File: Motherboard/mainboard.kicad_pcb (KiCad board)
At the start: 4 copper layers, 45 x 35 mm, 48 parts, among them IC1 BMX160, J1 Conn_01x01, J2 10118194-0001LF, J28 Conn_01x01, J29 Conn_01x01, J3 Micro_SD_Card, J30 Conn_01x01, J4 xf2m-2415-1a, J5 XF2M-1015-1A, SW1 KMR231NG LFS, U1 RFM95W-915S2, U2 ATSAMD51G_TQFN48, U3 DRV8848, U4 TPS82740BSIPR, U5 DRV8848, U6 MAX708RESA-T, U8 RFM95W-915S2, X1 ANTENNA_U.FL, X2 ANTENNA_U.FL

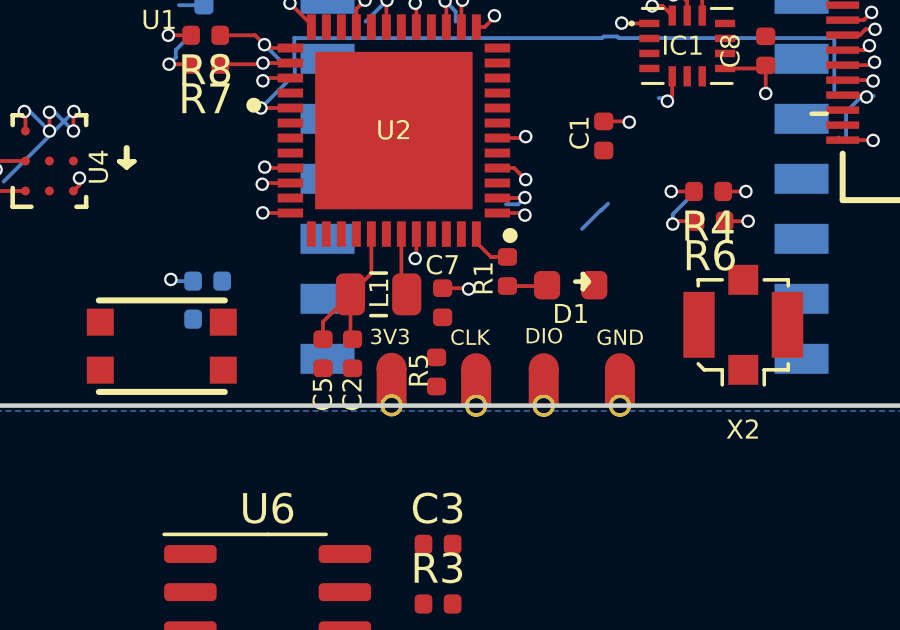
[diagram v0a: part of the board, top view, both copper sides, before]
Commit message: added traces for J29, J28, J30
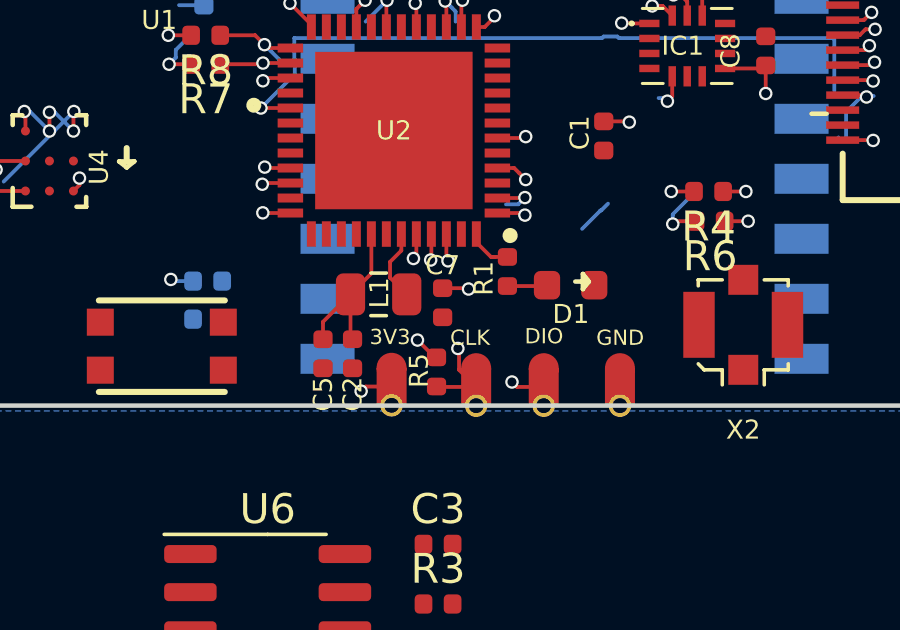
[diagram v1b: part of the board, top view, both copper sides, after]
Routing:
- net /SWCLK: track 0.00 -> 7.06 mm, vias 0 -> 2
- net /SWDIO: track 0.00 -> 6.97 mm, vias 0 -> 2
- net +3V3: track 18.4 -> 20.4 mm, vias 17 -> 19
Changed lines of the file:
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@@
     (thickness 1.2)
     (drawings 35)
-    (tracks 395)
+    (tracks 423)
     (zones 0)
     (modules 48)
@@
   (segment (start 82.9097 99.5086) (end 83.6295 99.5086) (width 0.127) (layer Top) (net 4))
   (segment (start 82.6597 99.2586) (end 82.9097 99.5086) (width 0.127) (layer Top) (net 4))
+  (segment (start 101.6889 108.4199) (end 101.5238 108.2548) (width 0.127) (layer Top) (net 5))
+  (via (at 101.5238 108.2548) (size 0.45) (drill 0.3) (layers Top Bottom) (net 5))
+  (segment (start 102.58298 108.4199) (end 101.6889 108.4199) (width 0.127) (layer Top) (net 5))
+  (segment (start 99.3368 104.1628) (end 99.3902 104.2162) (width 0.127) (layer Top) (net 5))
+  (segment (start 99.3368 103.3228) (end 99.3368 104.1628) (width 0.127) (layer Top) (net 5))
+  (via (at 99.3902 104.2162) (size 0.45) (drill 0.3) (layers Top Bottom) (net 5))
+  (segment (start 99.3902 106.1212) (end 101.5238 108.2548) (width 0.127) (layer In2.Cu) (net 5))
+  (segment (start 99.3902 104.2162) (end 99.3902 106.1212) (width 0.127) (layer In2.Cu) (net 5))
+  (segment (start 99.02458 108.4199) (end 99.0092 108.40452) (width 0.127) (layer Top) (net 6))
+  (segment (start 100.33 108.4199) (end 99.02458 108.4199) (width 0.127) (layer Top) (net 6))
+  (via (at 99.7204 107.1372) (size 0.45) (drill 0.3) (layers Top Bottom) (net 6))
+  (segment (start 99.75929 107.84919) (end 99.75929 107.17609) (width 0.127) (layer Top) (net 6))
+  (segment (start 99.75929 107.17609) (end 99.7204 107.1372) (width 0.127) (layer Top) (net 6))
+  (segment (start 100.33 108.4199) (end 99.75929 107.84919) (width 0.127) (layer Top) (net 6))
+  (via (at 98.813811 104.189379) (size 0.45) (drill 0.3) (layers Top Bottom) (net 6))
+  (segment (start 98.8368 104.16639) (end 98.813811 104.189379) (width 0.127) (layer Top) (net 6))
+  (segment (start 99.7204 107.1372) (end 98.813811 106.230611) (width 0.127) (layer In2.Cu) (net 6))
+  (segment (start 98.813811 106.230611) (end 98.813811 104.507577) (width 0.127) (layer In2.Cu) (net 6))
+  (segment (start 98.8368 103.3228) (end 98.8368 104.16639) (width 0.127) (layer Top) (net 6))
+  (segment (start 98.813811 104.507577) (end 98.813811 104.189379) (width 0.127) (layer In2.Cu) (net 6))
   (segment (start 100.8258 104.0868) (end 100.9514 104.0868) (width 0.127) (layer Top) (net 7))
   (segment (start 100.3368 103.5978) (end 100.8258 104.0868) (width 0.127) (layer Top) (net 7))
@@
   (segment (start 102.6643 105.0568) (end 102.6921 105.029) (width 0.127) (layer Top) (net 12))
   (segment (start 101.3714 105.0568) (end 102.6643 105.0568) (width 0.127) (layer Top) (net 12))
-  (segment (start 97.8368 105.1543) (end 98.0163 105.3338) (width 0.127) (layer Top) (net 18))
-  (segment (start 97.8368 103.3228) (end 97.8368 105.1543) (width 0.127) (layer Top) (net 18))
+  (segment (start 97.8368 103.8748) (end 97.460063 104.251537) (width 0.127) (layer Top) (net 18))
+  (segment (start 97.460063 104.251537) (end 97.460063 104.777563) (width 0.127) (layer Top) (net 18))
+  (segment (start 97.460063 104.777563) (end 98.0163 105.3338) (width 0.127) (layer Top) (net 18))
+  (segment (start 97.8368 103.3228) (end 97.8368 103.8748) (width 0.127) (layer Top) (net 18))
   (via (at 98.298 95.63101) (size 0.45) (drill 0.3) (layers Top Bottom) (net 20))
   (segment (start 98.3368 96.4228) (end 98.3368 95.66981) (width 0.127) (layer Top) (net 20))
   (segment (start 98.3368 95.66981) (end 98.298 95.63101) (width 0.127) (layer Top) (net 20))
-  (via (at 98.298 104.14) (size 0.45) (drill 0.3) (layers Top Bottom) (net 20))
-  (segment (start 98.3368 104.1012) (end 98.298 104.14) (width 0.127) (layer Top) (net 20))
-  (segment (start 98.3368 103.3228) (end 98.3368 104.1012) (width 0.127) (layer Top) (net 20))
   (via (at 101.981 100.076) (size 0.45) (drill 0.3) (layers Top Bottom) (net 20))
   (segment (start 101.9342 100.1228) (end 101.981 100.076) (width 0.127) (layer Top) (net 20))
@@
   (segment (start 107.6428 102.8954) (end 106.977622 102.8954) (width 0.127) (layer Top) (net 20))
   (segment (start 106.8832 102.6668) (end 106.8832 102.671624) (width 0.127) (layer Bottom) (net 20))
+  (via (at 98.3742 106.8578) (size 0.45) (drill 0.3) (layers Top Bottom) (net 20))
+  (segment (start 98.95092 107.43452) (end 98.3742 106.8578) (width 0.127) (layer Top) (net 20))
+  (segment (start 99.0092 107.43452) (end 98.95092 107.43452) (width 0.127) (layer Top) (net 20))
+  (via (at 96.4946 108.5596) (size 0.45) (drill 0.3) (layers Top Bottom) (net 20))
+  (segment (start 96.647 108.4072) (end 96.4946 108.5596) (width 0.127) (layer Top) (net 20))
+  (segment (start 97.5106 108.4072) (end 96.647 108.4072) (width 0.127) (layer Top) (net 20))
+  (segment (start 98.3368 103.3228) (end 98.3368 104.040464) (width 0.127) (layer Top) (net 20))
+  (via (at 98.239074 104.13819) (size 0.45) (drill 0.3) (layers Top Bottom) (net 20))
+  (segment (start 98.3368 104.040464) (end 98.239074 104.13819) (width 0.127) (layer Top) (net 20))
   (segment (start 83.909698 101.888798) (end 83.6295 101.6086) (width 0.127) (layer Top) (net 21))
   (segment (start 85.305999 101.888798) (end 83.909698 101.888798) (width 0.127) (layer Top) (net 21))

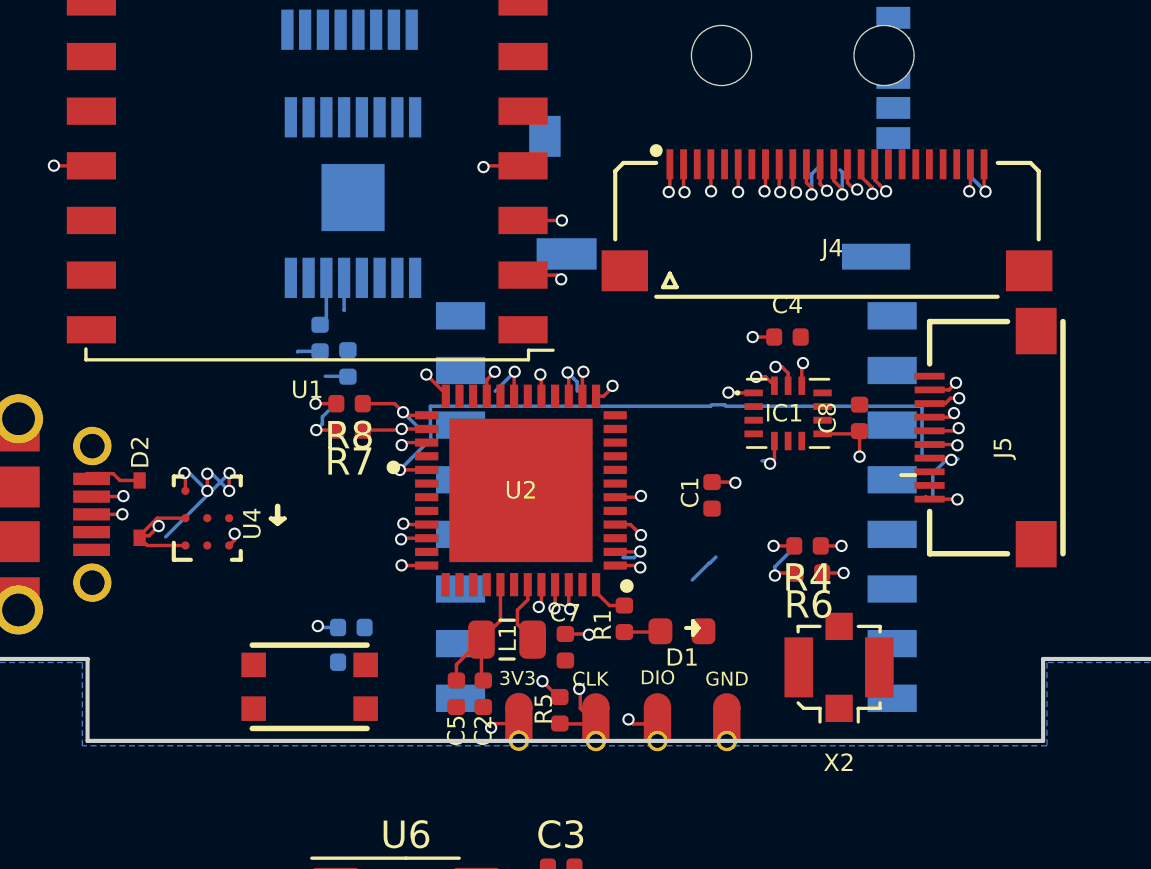
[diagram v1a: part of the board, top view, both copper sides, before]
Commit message: deleted accidental bottom traces on bottom of board
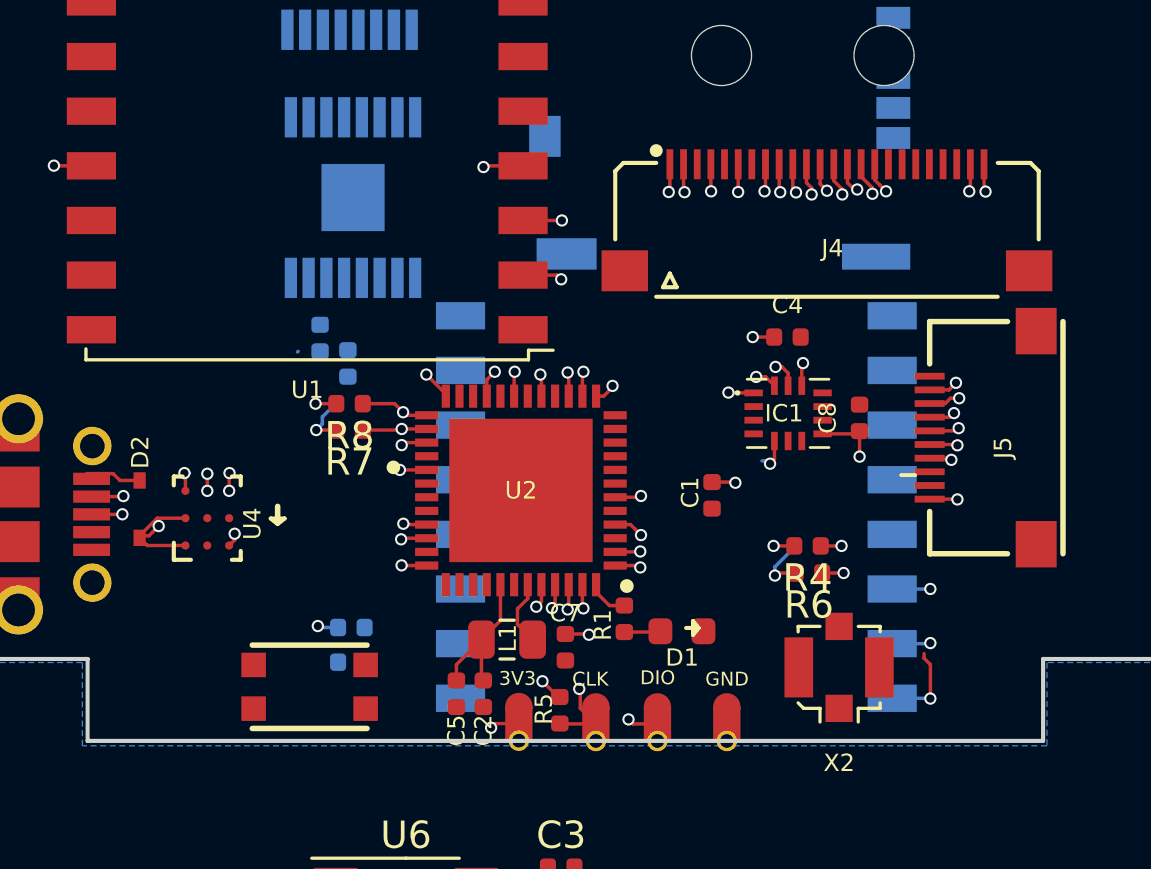
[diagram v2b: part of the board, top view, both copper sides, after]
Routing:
- net EN_CAM: track 45.4 -> 22.8 mm
- net Net-(D2-Pad1): track 20.4 -> 15.3 mm
- net RF_DIO2: track 0.00 -> 3.14 mm, vias 0 -> 1
- net GND: track 3.63 -> 0.82 mm
- net RF_DIO0: track 0.00 -> 2.28 mm, vias 0 -> 2
- net BATT_N: track 14.4 -> 12.3 mm
- net SCL2: track 5.49 -> 3.75 mm
- net Net-(C13-Pad2): track 1.82 -> 0.33 mm
- net RF_DIO1: track 0.00 -> 1.41 mm, vias 0 -> 1
- net SDA1: track 27.4 -> 26.2 mm
- net BURN2: track 2.37 -> 1.18 mm
- net MISO: track 17.4 -> 16.4 mm
- net RF_CS: track 1.91 -> 0.90 mm
- net BATT_P: track 14.5 -> 13.7 mm
- net SCL1: track 25.4 -> 24.6 mm

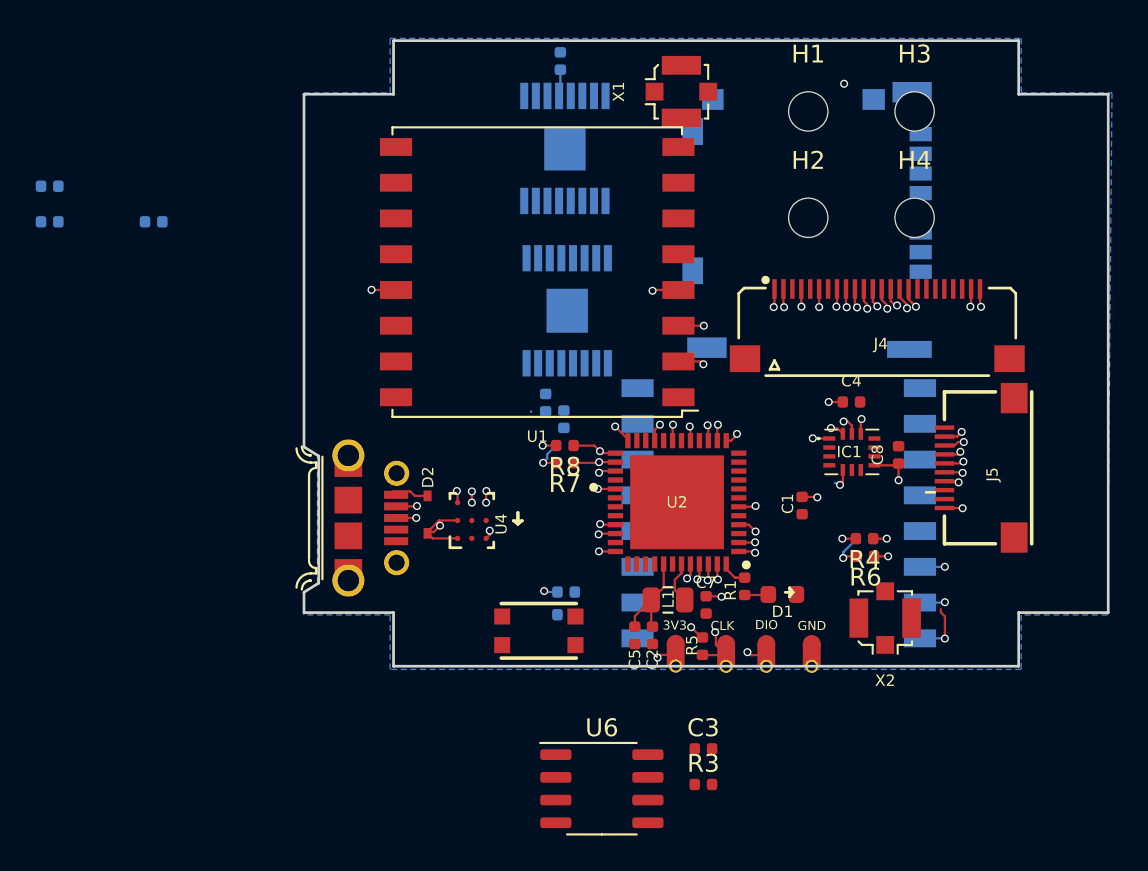
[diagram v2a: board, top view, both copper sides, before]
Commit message: updated position of UHF on bottom of board to not overlap MCU
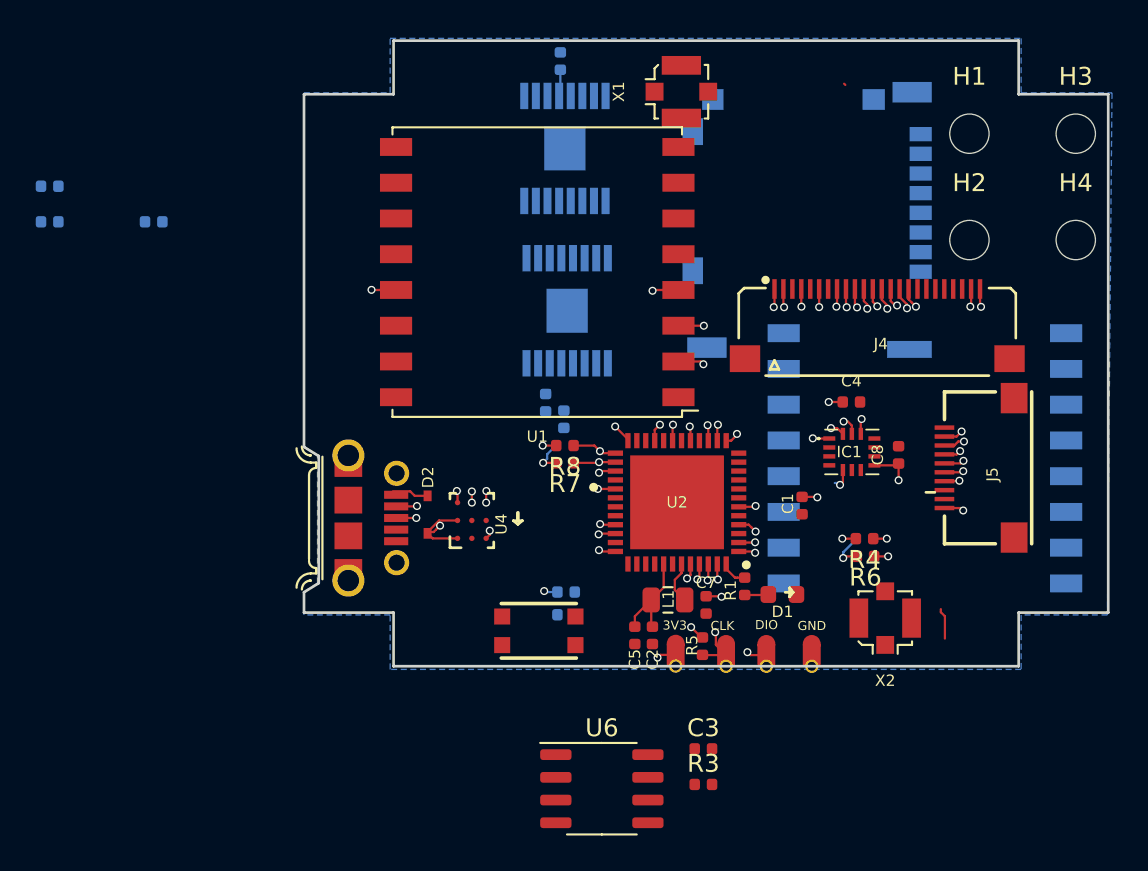
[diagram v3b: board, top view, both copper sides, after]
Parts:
- moved H3 9.10 mm to (119.9, 79.2)
- moved H4 9.10 mm to (119.9, 85.2)
- moved H1 9.10 mm to (113.9, 79.2)
- moved H2 9.10 mm to (113.9, 85.2)
- moved U8 8.74 mm to (111.5, 97.4)
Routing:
- net RF_DIO1: track 1.41 -> 0.00 mm, vias 1 -> 0
- net RF_DIO2: track 3.14 -> 1.74 mm, vias 1 -> 0
- net RF_DIO0: track 2.28 -> 0.88 mm, vias 2 -> 1
- net SDA1: track 26.2 -> 25.2 mm
- net SCL1: track 24.6 -> 23.9 mm
- net +3V3: vias 19 -> 18

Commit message: added watchdog timer footprint to PCB layout
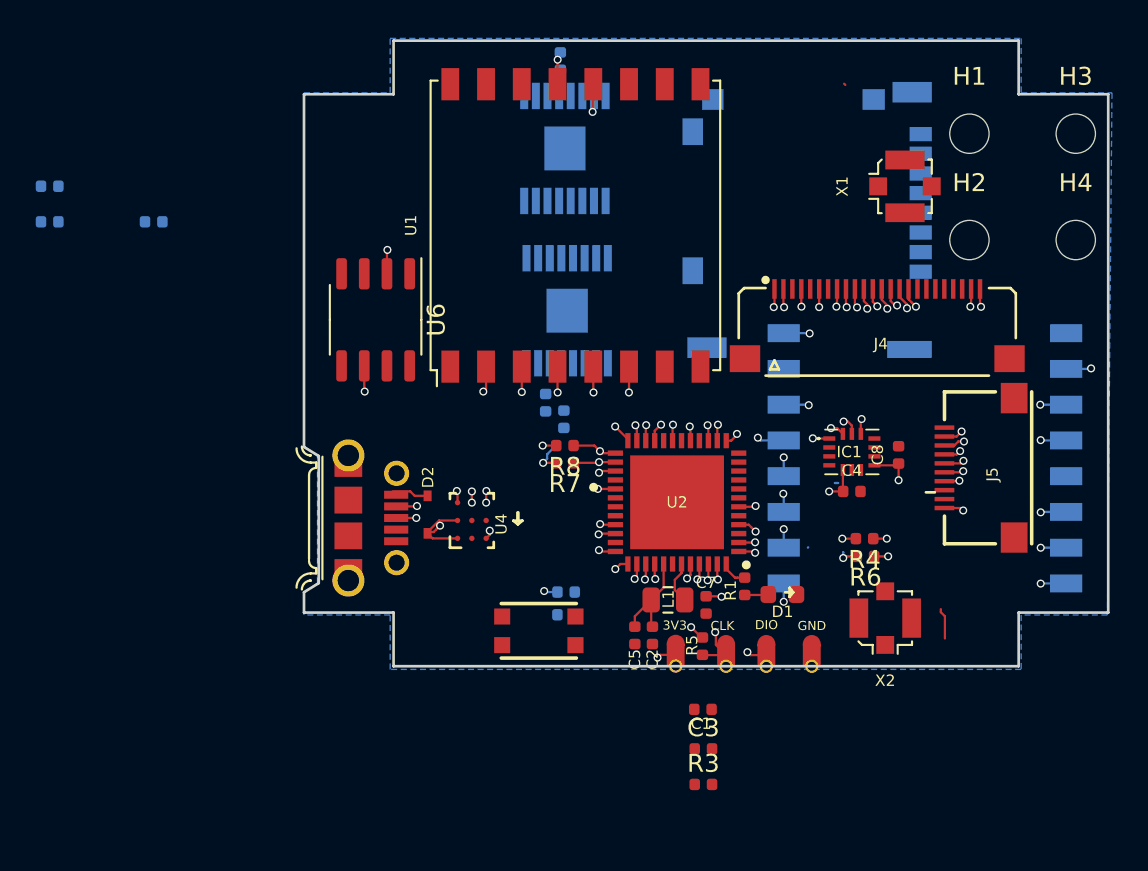
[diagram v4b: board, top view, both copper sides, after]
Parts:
- moved U6 29.1 mm to (80.7, 89.7), turned to 270 degrees
- moved X1 13.6 mm to (110.3, 82.2)
- moved C1 12.7 mm to (99.0, 111.5), turned to 0 degrees
- moved C4 5.00 mm to (107.4, 99.3)
- moved U1 3.37 mm to (91.9, 84.4), turned to 90 degrees
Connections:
- U2 pad 20: WDT_WDI -> Net-(U2-Pad20)
- U2 pad 37: Net-(U2-Pad37) -> WDT_WDI
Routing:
- net SCK: track 32.2 -> 25.6 mm, vias 4 -> 5
- net MOSI: track 24.2 -> 18.4 mm, vias 4 -> 5
- net MISO: track 16.5 -> 20.6 mm, vias 4 -> 5
- net GND: track 0.79 -> 4.68 mm, vias 1 -> 4
- net RF_DIO3: track 0.00 -> 2.35 mm, vias 0 -> 2
- net RF_DIO2: track 1.74 -> 4.05 mm, vias 0 -> 2
- net RF_DIO1: track 0.00 -> 2.31 mm, vias 0 -> 2
- net RF_BUSY: track 0.00 -> 2.31 mm, vias 0 -> 2
- net WDT_WDI: track 0.00 -> 2.27 mm, vias 0 -> 2
- net RF2_BUSY: track 0.00 -> 1.56 mm, vias 0 -> 1
- net CS_RF1: track 0.00 -> 1.51 mm, vias 0 -> 1
- net CS_RF2: track 0.00 -> 1.45 mm, vias 0 -> 1
- net RF2_RST: track 0.00 -> 1.45 mm, vias 0 -> 1
- net RF_RST: track 1.01 -> 2.46 mm, vias 1 -> 2
- net RF_DIO0: track 0.88 -> 2.32 mm, vias 1 -> 2
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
